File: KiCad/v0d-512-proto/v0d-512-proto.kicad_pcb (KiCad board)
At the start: 2 copper layers, 90 x 56.8 mm, 19 parts, among them U1 SST39SF040, U2 62256/628128, U3 74HC139, U4 74HC191, U5 74HC4520, U6 74HC191, U7 74HC191, U8 74HC670

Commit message: fix issues
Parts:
- added JP2: SolderJumper_2_Open, Jumper:SolderJumper-2_P1.3mm_Open_Pad1.0x1.5mm, B.Cu at (162.6, 92.7)
- added JP3: SolderJumper_2_Open, Jumper:SolderJumper-2_P1.3mm_Open_Pad1.0x1.5mm, B.Cu at (162.5, 90.2)
- added JP4: SolderJumper_2_Open, Jumper:SolderJumper-2_P1.3mm_Open_Pad1.0x1.5mm, B.Cu at (162.5, 87.6)
- added JP5: SolderJumper_2_Open, Jumper:SolderJumper-2_P1.3mm_Open_Pad1.0x1.5mm, B.Cu at (162.6, 85.1)
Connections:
- net /rfAUDIO renamed Net-(H1-cAUDIO)
- JP1 pad 3: /pA13 -> VCC
- U6 pad 5: GND -> VCC
- U7 pad 5: GND -> VCC
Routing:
- net VCC: track 290.0 -> 311.7 mm
- net /pBank1: track 35.2 -> 39.0 mm, vias 1 -> 2
- net /pA11: track 86.2 -> 89.3 mm, vias 3 -> 5
- net /pA13: track 77.5 -> 79.2 mm
- net /pBank2: track 24.0 -> 25.2 mm, vias 0 -> 1
- net /cD3: track 98.9 -> 97.6 mm
- net /pA12: track 65.7 -> 66.9 mm
- net /pBank3: track 46.4 -> 46.6 mm, vias 1 -> 2
- net GND: vias 87 -> 82
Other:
- board text added: "128k"
- board text added: "32k"
- board text added: "8K"
- board text removed: "11"
- board text removed: "13"

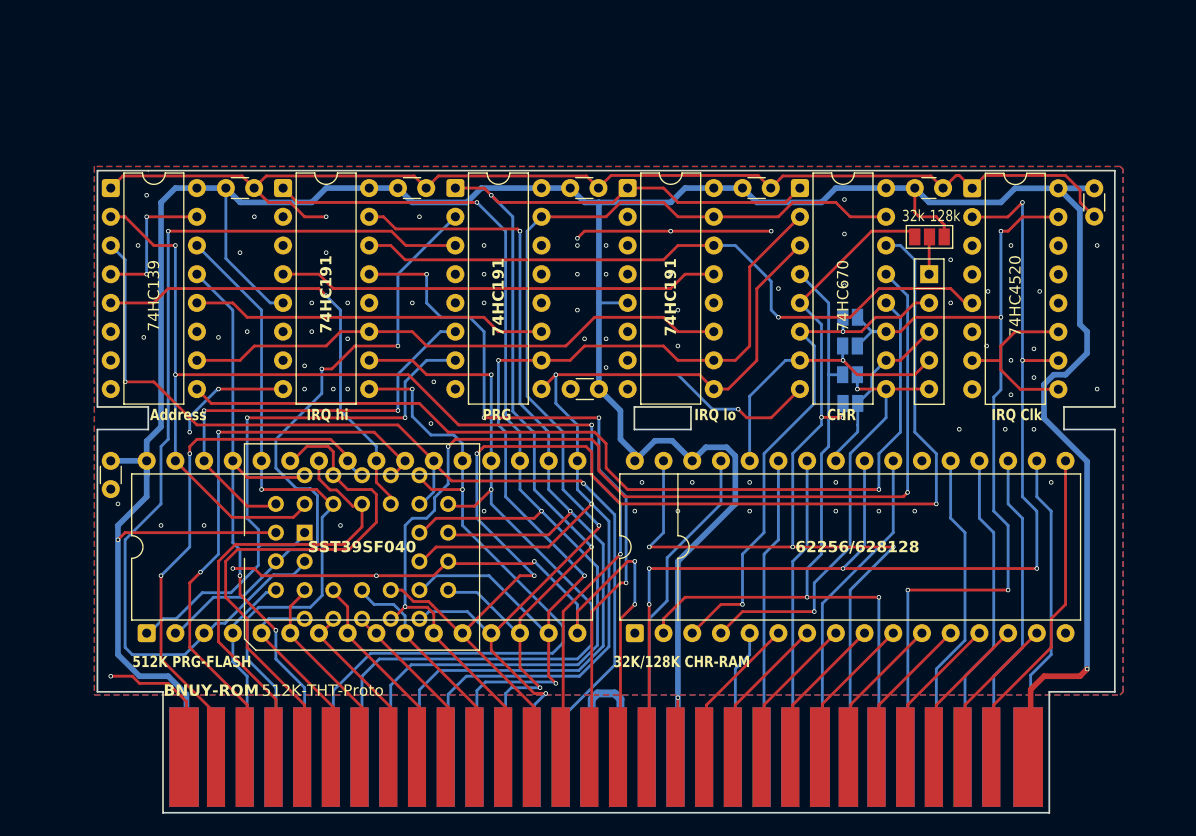
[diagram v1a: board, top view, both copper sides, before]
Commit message: Update to latest pcb version, README tweaks
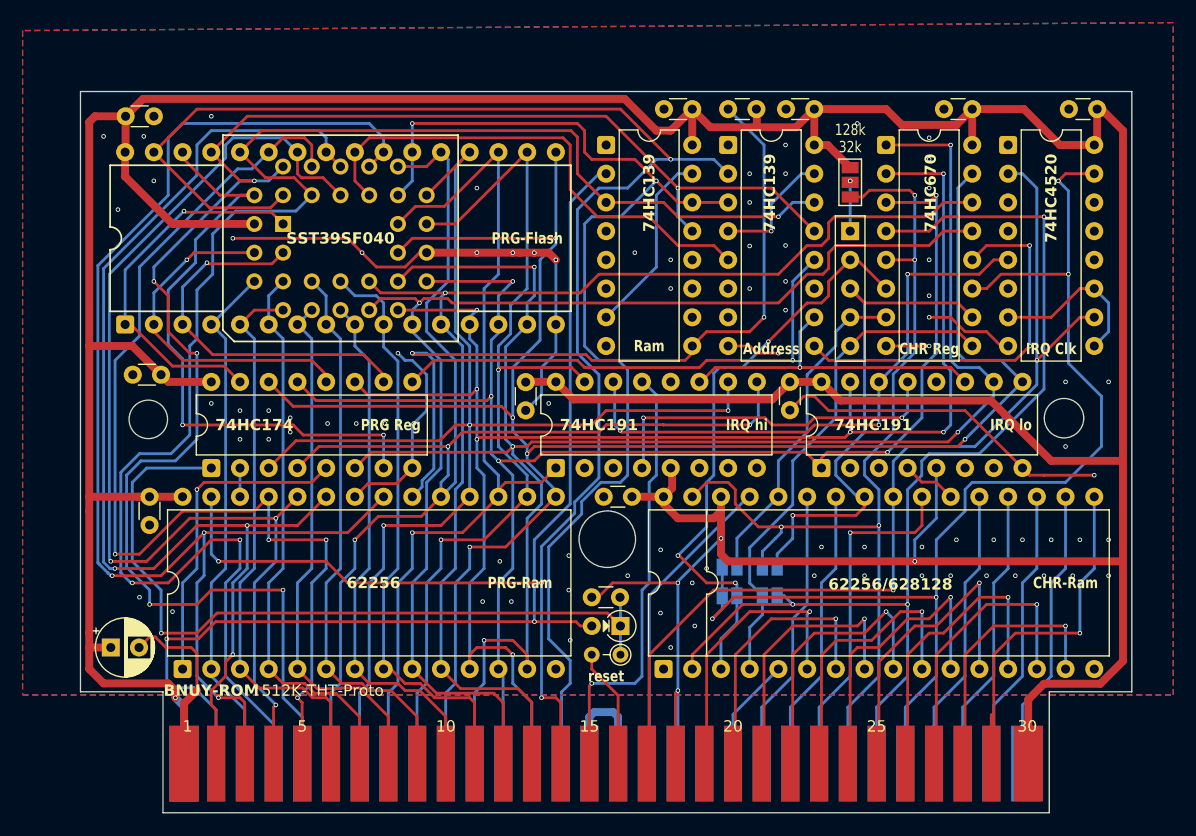
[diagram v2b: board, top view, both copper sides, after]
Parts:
- added C10: C, Capacitor_THT:C_Disc_D3.0mm_W1.6mm_P2.50mm, F.Cu at (184.4, 66.7)
- added C11: C, Capacitor_THT:C_Disc_D3.0mm_W1.6mm_P2.50mm, F.Cu at (143.3, 101.0)
- added C12: 1nF, Capacitor_THT:C_Disc_D3.0mm_W1.6mm_P2.50mm, F.Cu at (139.7, 109.9)
- added C13: 1nF, Capacitor_THT:C_Disc_D3.0mm_W1.6mm_P2.50mm, F.Cu at (154.3, 66.7)
- added C9: C_Polarized, Capacitor_THT:CP_Radial_D5.0mm_P2.50mm, F.Cu at (97.2, 114.3)
- added D1: 1N4148, PCM_Diode_THT_AKL:D_DO-35_SOD27_P2.54mm_Vertical_AnodeUp, F.Cu at (142.2, 112.4)
- added R1: 4.7KΩ, Resistor_THT:R_Axial_DIN0204_L3.6mm_D1.6mm_P2.54mm_Vertical, F.Cu at (142.2, 114.9)
- added U10: 62256, Package_DIP:DIP-28_W15.24mm, F.Cu at (103.5, 116.2)
- added U9: 74HC139, Package_DIP:DIP-16_W7.62mm, F.Cu at (141.0, 69.8)
- J1: renamed from H1; value Famicom_Cartridge_Edge -> Famicom Cartridge Connector
- U4: value 74HC191 -> 74HC174
- moved C5 87.9 mm to (100.6, 101.0)
- moved U3 54.7 mm to (151.8, 69.8)
- moved C2 38.8 mm to (101.6, 90.2)
- moved C7 38.7 mm to (157.2, 90.8), turned to -90 degrees
- moved U7 34.6 mm to (136.5, 98.4), turned to 90 degrees
- moved U4 32.9 mm to (106.0, 98.4), turned to 90 degrees
- moved C3 31.6 mm to (133.9, 90.8), turned to -90 degrees
- moved C1 30.5 mm to (98.5, 67.3), turned to 0 degrees
- moved U6 30.1 mm to (160.0, 98.4), turned to 90 degrees
- moved U1 27.4 mm to (112.4, 76.8)
- moved JP5 26.8 mm to (151.9, 109.7), turned to 180 degrees
- moved JP4 22.3 mm to (151.9, 107.2), turned to 180 degrees
- moved JP3 20.8 mm to (155.4, 109.7), turned to 0 degrees
- moved JP2 16.1 mm to (155.4, 107.2)
- moved C4 12.9 mm to (148.6, 66.7), turned to 180 degrees
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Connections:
- net /R~{W} renamed /CPU.R/~{W}
- net /cA0 renamed /CPU.A0
- net /cA1 renamed /CPU.A1
- net /cA10 renamed /CPU.A10
- net /cA11 renamed /CPU.A11
- net /cA12 renamed /CPU.A12
- net /cA13 renamed /CPU.A13
- net /cA14 renamed /CPU.A14
- net /cA2 renamed /CPU.A2
- net /cA3 renamed /CPU.A3
- net /cA4 renamed /CPU.A4
- net /cA5 renamed /CPU.A5
- net /cA6 renamed /CPU.A6
- net /cA7 renamed /CPU.A7
- net /cA8 renamed /CPU.A8
- net /cA9 renamed /CPU.A9
- net /cD4 renamed /CPU.D4
- net /cD5 renamed /CPU.D5
- net /pA0 renamed /PPU.A0
- net /pA1 renamed /PPU.A1
- net /pA10 renamed /PPU.A10
- net /pA11 renamed /PPU.A11
- net /pA12 renamed /PPU.A12
- net /pA13 renamed /PPU.A13
- net /pA2 renamed /PPU.A2
- net /pA3 renamed /PPU.A3
- net /pA4 renamed /PPU.A4
- net /pA5 renamed /PPU.A5
- net /pA6 renamed /PPU.A6
- net /pA7 renamed /PPU.A7
- net /pA8 renamed /PPU.A8
- net /pA9 renamed /PPU.A9
- net /pBank0 renamed /CHR.B0
- net /pBank1 renamed /CHR.B1
- net /pBank2 renamed /CHR.B2
- net /pBank3 renamed /CHR.B3
- net /pD0 renamed /PPU.D0
- net /pD1 renamed /PPU.D1
- net /pD2 renamed /PPU.D2
- net /pD3 renamed /PPU.D3
- net /pD4 renamed /PPU.D4
- net /pD5 renamed /PPU.D5
- net /pD6 renamed /PPU.D6
- net /pD7 renamed /PPU.D7
- net /~{pRD} renamed /PPU.~{Rd}
- net /~{pWR} renamed /PPU.~{Wr}
- J1 pad 36: /cD7 -> /CPU.D7
- J1 pad 37: /cD6 -> /CPU.D6
- J1 pad 40: /cD3 -> /CPU.D3
- J1 pad 41: /cD2 -> /CPU.D2
- J1 pad 42: /cD1 -> /CPU.D1
- J1 pad 43: /cD0 -> /CPU.D0
- U1 pad 1: /cBank3 -> /PRG.B3
- U1 pad 13: /cD0 -> /CPU.D0
- U1 pad 14: /cD1 -> /CPU.D1
- U1 pad 15: /cD2 -> /CPU.D2
- U1 pad 17: /cD3 -> /CPU.D3
- U1 pad 2: /cBank1 -> /PRG.B1
- U1 pad 20: /cD6 -> /CPU.D6
- U1 pad 21: /cD7 -> /CPU.D7
- U1 pad 3: /cBank0 -> /PRG.B0
- U1 pad 30: /cBank2 -> /PRG.B2
- U4 pad 1: /cD1 -> /~{RESET}
- U4 pad 10: /cD2 -> /PRG.B0
- U4 pad 11: /~{prgWR} -> /CPU.D0
- U4 pad 12: unconnected-(U4-Tc-Pad12) -> /PRG.B1
- U4 pad 13: unconnected-(U4-Rc-Pad13) -> /CPU.D1
- U4 pad 14: GND -> /CPU.D3
- U4 pad 15: /cD0 -> /PRG.B3
- U4 pad 2: /cBank1 -> /PRG.B6
- U4 pad 3: /cBank0 -> /CPU.D6
- U4 pad 4: GND -> /CPU.D7
- U4 pad 5: GND -> /PRG.B7
- U4 pad 6: /cBank2 -> /CPU.D2
- U4 pad 7: /cBank3 -> /PRG.B2
- U4 pad 9: /cD3 -> /~{prgWR}
- U6 pad 1: /cD1 -> /CPU.D1
- U6 pad 10: /cD2 -> /CPU.D2
- U6 pad 15: /cD0 -> /CPU.D0
- U6 pad 9: /cD3 -> /CPU.D3
- U7 pad 10: /cD6 -> /CPU.D6
- U7 pad 9: /cD7 -> /CPU.D7
- U8 pad 1: /cD1 -> /CPU.D2
- U8 pad 15: /cD0 -> /CPU.D3
- U8 pad 2: /cD2 -> /CPU.D0
- U8 pad 3: /cD3 -> /CPU.D1
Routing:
- net /CPU.D3: track 0.00 -> 170.2 mm, vias 0 -> 5
- net /CPU.D2: track 0.00 -> 157.1 mm, vias 0 -> 5
- net /CPU.D0: track 0.00 -> 141.4 mm, vias 0 -> 7
- net /CPU.D1: track 0.00 -> 135.6 mm, vias 0 -> 5
- net VCC: track 311.7 -> 443.0 mm, vias 3 -> 5
- net /CPU.D7: track 0.00 -> 117.2 mm, vias 0 -> 3
- net /CPU.D6: track 0.00 -> 112.3 mm, vias 0 -> 3
- net /cD1: track 100.1 -> 0.00 mm, vias 3 -> 0
- net /cD0: track 98.1 -> 0.00 mm, vias 2 -> 0
- net /cD2: track 97.9 -> 0.00 mm, vias 3 -> 0
- net /cD3: track 97.6 -> 0.00 mm, vias 2 -> 0
- net /CPU.A14: track 53.3 -> 148.0 mm, vias 2 -> 6
- net /M2: track 0.00 -> 94.3 mm, vias 0 -> 2
- net /CPU.A13: track 59.8 -> 144.2 mm, vias 1 -> 3
- net /cBank0: track 83.8 -> 0.00 mm, vias 1 -> 0
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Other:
- board size 90 x 56.8 mm -> 93 x 53.1 mm
- board text added: "C"
- board text added: "CHR Reg"
- board text added: "CHR-Ram"
- board text added: "PRG Reg"
- board text added: "PRG-Flash"
- board text added: "PRG-Ram"
- board text added: "R"
- board text added: "Ram"
- board text added: "github.com/smaldragon/BNUY-ROM"
- board text added: "reset"
- board text removed: "32K/128K CHR-RAM"
- board text removed: "512K PRG-FLASH"
- board text removed: "CHR"
- board text removed: "PRG"
